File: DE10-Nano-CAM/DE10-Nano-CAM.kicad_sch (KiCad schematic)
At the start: 16 parts, among them J1 DF40C-100DS-0.4V_51_, J2 DF40C-100DS-0.4V_51_, J3 MEM2075-00-140-01-A, J4 Conn_02x20_Odd_Even, J5 52271-1579

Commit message: changed pcb
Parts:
- added R5, R6: 4.7k, Resistor_SMD:R_0603_1608Metric, symbol CAN-Adapter_3.2korr_0622-eagle-import:R-EU_R0603
- added R7, R8: DNP, Resistor_SMD:R_0603_1608Metric, symbol CAN-Adapter_3.2korr_0622-eagle-import:R-EU_R0603
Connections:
- net +3.3V: now also R5.2, R6.2, R7.2, R8.2
- net DATA_11: now also J4.21 (Pin_21); no longer J4.17 (Pin_17)
- net DDMI0_CLK_N: no longer J5.8
- net DDMI0_CLK_P: no longer J5.9
- net SCL0: now also R7.1
- net SDA0: now also R8.1
- net LVDS0_D0_P: now reaches J4.19 (Pin_19)
- net LVDS0_D0_P: now also J1.17
- net SCL_DE10: now reaches J4.31 (Pin_31)
- net SCL_DE10: now also R5.1
- net SDA_DE10: now reaches J4.32 (Pin_32)
- net SDA_DE10: now also R6.1
- net LVDS0_D1_N: now reaches J4.33 (Pin_33)
- net LVDS0_D1_N: now also J1.21
- net LVDS0_D2_N: now reaches J4.34 (Pin_34)
- net LVDS0_D2_N: now also J1.33
- net LVDS0_D1_P: now reaches J4.35 (Pin_35)
- net LVDS0_D1_P: now also J1.23
- net LVDS0_D2_P: now reaches J4.36 (Pin_36)
- net LVDS0_D2_P: now also J1.35
- net LVDS0_C_N: now reaches J4.37 (Pin_37)
- net LVDS0_C_N: now also J1.27
- net LVDS0_D3_N: now reaches J4.38 (Pin_38)
- net LVDS0_D3_N: now also J1.39
- net LVDS0_C_P: now reaches J4.39 (Pin_39)
- net LVDS0_C_P: now also J1.29
- net LVDS0_D3_P: now reaches J4.40 (Pin_40)
- net LVDS0_D3_P: now also J1.41
- net LVDS0_D0_N: now reaches J1.15
- net LVDS0_D0_N: now also J4.17 (Pin_17)
- new net LVDS1_C_N: J5.8
- new net LVDS1_C_P: J5.9
- no-connect marks 131 -> 108
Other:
- note added: "CONNECT TO WHERE?"
- note added: "Diff tuned to 14mm Diff Skew tuned"

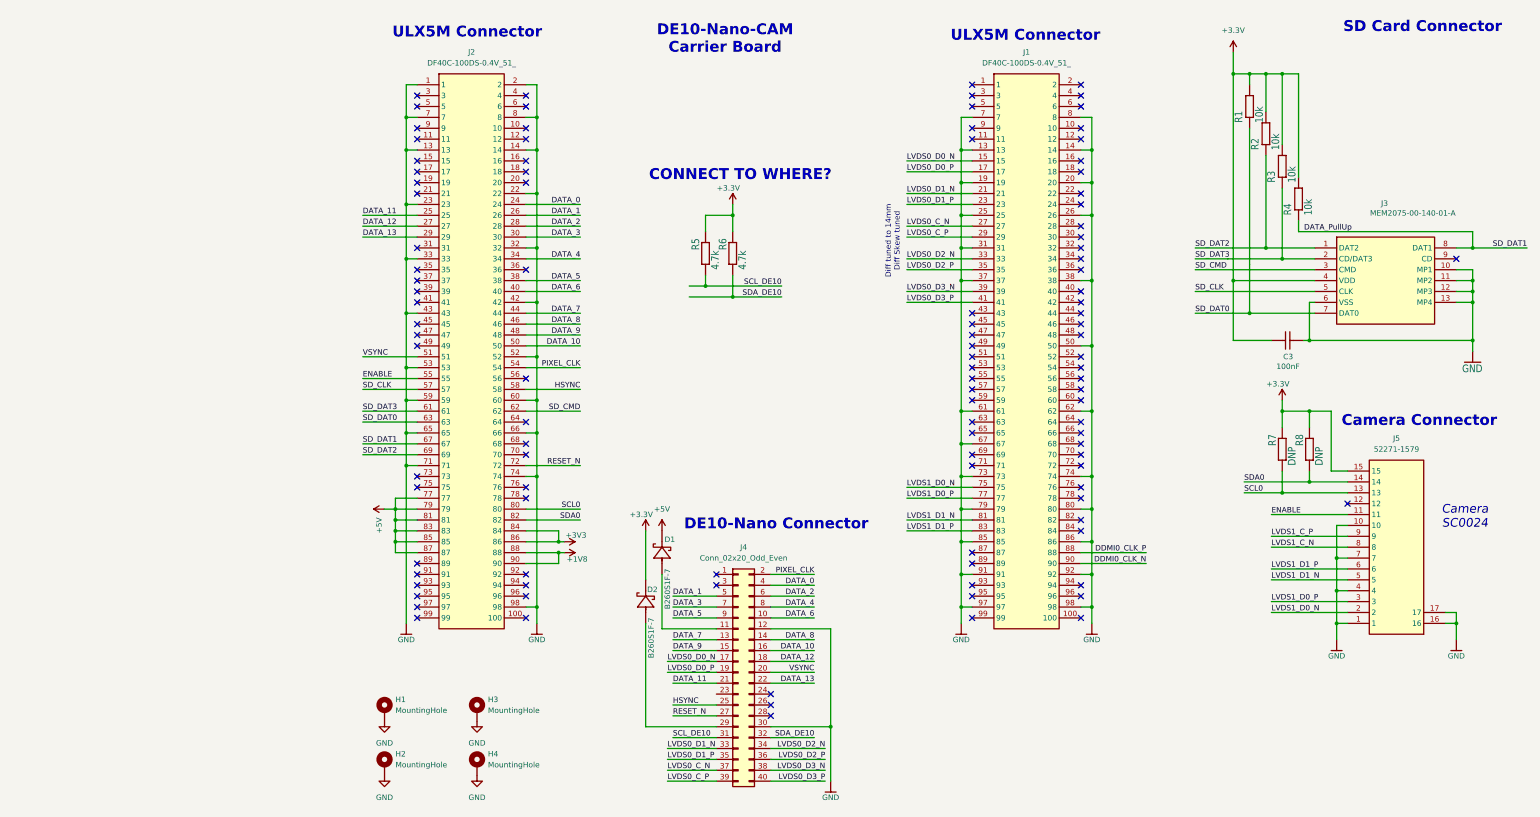
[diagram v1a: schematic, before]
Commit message: changes to DE10 schematic (GPIO)
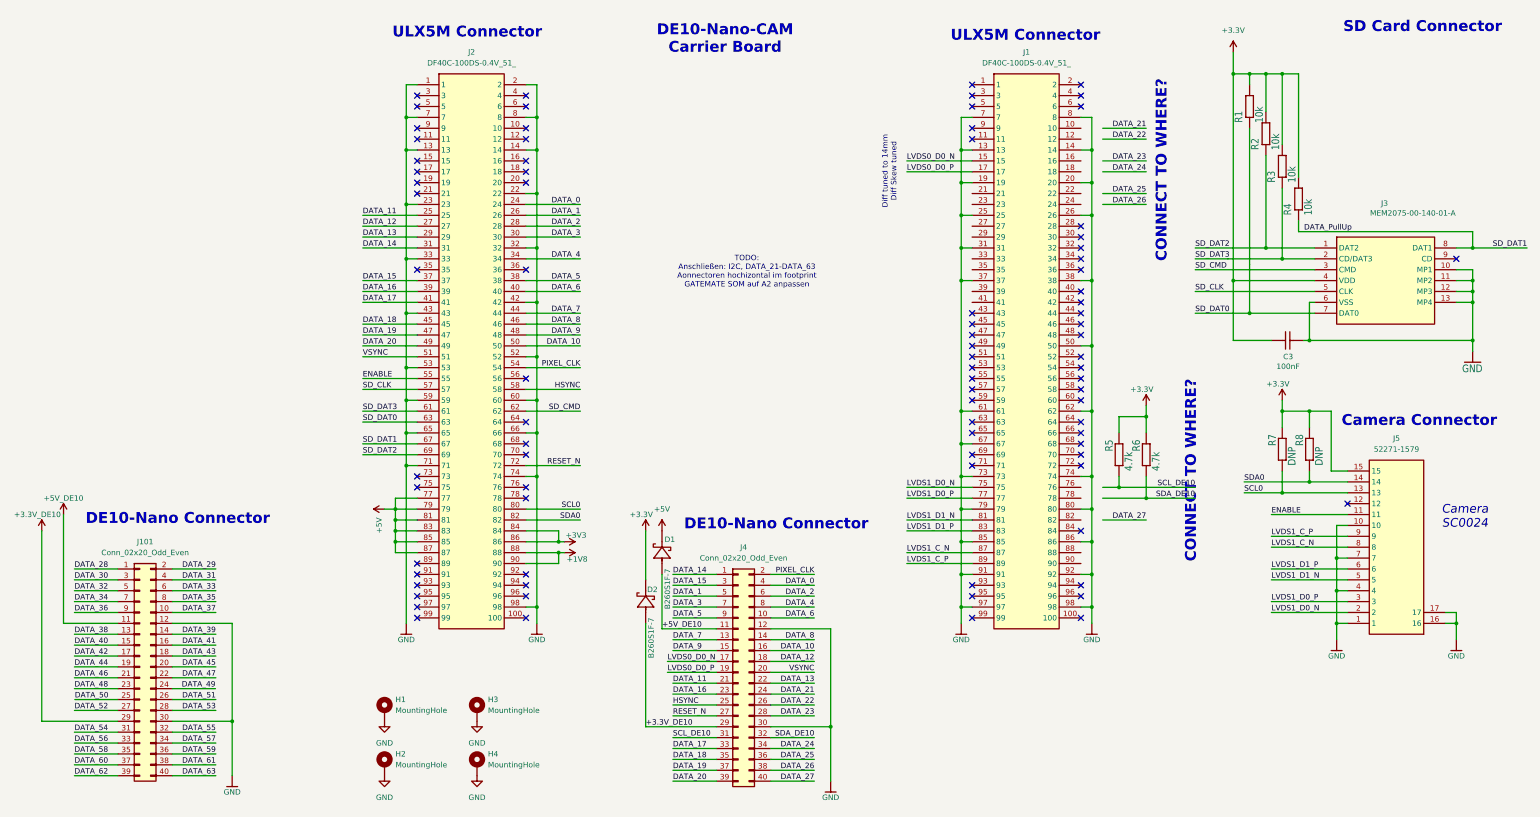
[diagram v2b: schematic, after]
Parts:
- added J101: Conn_02x20_Odd_Even, Connector_PinSocket_2.54mm:PinSocket_2x20_P2.54mm_Vertical, symbol Connector_Generic:Conn_02x20_Odd_Even
- J4: footprint Connector_PinSocket_2.54mm:PinSocket_2x20_P2.54mm_Horizontal -> Connector_PinSocket_2.54mm:PinSocket_2x20_P2.54mm_Vertical
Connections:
- net GND: now also J101.12 (Pin_12), J101.30 (Pin_30)
- net LVDS1_C_N: now also J1.87
- net LVDS1_C_P: now also J1.89
- net +3.3V_DE10: now reaches D2.2, J4.29 (Pin_29)
- net +3.3V_DE10: now also J101.29 (Pin_29)
- net DATA_14: now reaches J2.31
- net DATA_14: now also J4.1 (Pin_1)
- net DATA_15: now reaches J2.37
- net DATA_15: now also J4.3 (Pin_3)
- net DATA_16: now reaches J2.39
- net DATA_16: now also J4.23 (Pin_23)
- net DATA_17: now reaches J2.41
- net DATA_17: now also J4.33 (Pin_33)
- net DATA_18: now reaches J2.45
- net DATA_18: now also J4.35 (Pin_35)
- net DATA_19: now reaches J2.47
- net DATA_19: now also J4.37 (Pin_37)
- net DATA_20: now reaches J2.49
- net DATA_20: now also J4.39 (Pin_39)
- net +5V_DE10: now reaches D1.2, J4.11 (Pin_11)
- net +5V_DE10: now also J101.11 (Pin_11)
- net DATA_21: now reaches J4.24 (Pin_24)
- net DATA_22: now reaches J4.26 (Pin_26)
- net DATA_23: now reaches J4.28 (Pin_28)
- net DDMI0_CLK_N: no longer names the net of J1.90
- net DDMI0_CLK_P: no longer names the net of J1.88
- net LVDS0_C_N: no longer names the net of J1.27
- net LVDS0_C_N: no longer J4.37 (Pin_37)
- net LVDS0_C_P: no longer names the net of J1.29
- net LVDS0_C_P: no longer J4.39 (Pin_39)
- net LVDS0_D1_N: no longer names the net of J1.21
- net LVDS0_D1_N: no longer J4.33 (Pin_33)
- net LVDS0_D1_P: no longer names the net of J1.23
- net LVDS0_D1_P: no longer J4.35 (Pin_35)
- net LVDS0_D2_N: no longer names the net of J1.33
- net LVDS0_D2_N: no longer J4.34 (Pin_34)
- net LVDS0_D2_P: no longer names the net of J1.35
- net LVDS0_D2_P: no longer J4.36 (Pin_36)
- net LVDS0_D3_N: no longer names the net of J1.39
- net LVDS0_D3_N: no longer J4.38 (Pin_38)
- net LVDS0_D3_P: no longer names the net of J1.41
- net LVDS0_D3_P: no longer J4.40 (Pin_40)
- new net DATA_24: J4.34 (Pin_34)
- new net DATA_25: J4.36 (Pin_36)
- new net DATA_26: J4.38 (Pin_38)
- new net DATA_27: J4.40 (Pin_40)
- new net DATA_28: J101.1 (Pin_1)
- new net DATA_29: J101.2 (Pin_2)
- new net DATA_30: J101.3 (Pin_3)
- new net DATA_31: J101.4 (Pin_4)
- new net DATA_32: J101.5 (Pin_5)
- new net DATA_33: J101.6 (Pin_6)
- new net DATA_34: J101.7 (Pin_7)
- new net DATA_35: J101.8 (Pin_8)
- new net DATA_36: J101.9 (Pin_9)
- new net DATA_37: J101.10 (Pin_10)
- new net DATA_38: J101.13 (Pin_13)
- new net DATA_39: J101.14 (Pin_14)
- new net DATA_40: J101.15 (Pin_15)
- new net DATA_41: J101.16 (Pin_16)
- new net DATA_42: J101.17 (Pin_17)
- new net DATA_43: J101.18 (Pin_18)
- new net DATA_44: J101.19 (Pin_19)
- new net DATA_45: J101.20 (Pin_20)
- new net DATA_46: J101.21 (Pin_21)
- new net DATA_47: J101.22 (Pin_22)
- new net DATA_48: J101.23 (Pin_23)
- new net DATA_49: J101.24 (Pin_24)
- new net DATA_50: J101.25 (Pin_25)
- new net DATA_51: J101.26 (Pin_26)
- new net DATA_52: J101.27 (Pin_27)
- new net DATA_53: J101.28 (Pin_28)
- new net DATA_54: J101.31 (Pin_31)
- new net DATA_55: J101.32 (Pin_32)
- new net DATA_56: J101.33 (Pin_33)
- new net DATA_57: J101.34 (Pin_34)
- new net DATA_58: J101.35 (Pin_35)
- new net DATA_59: J101.36 (Pin_36)
- new net DATA_60: J101.37 (Pin_37)
- new net DATA_61: J101.38 (Pin_38)
- new net DATA_62: J101.39 (Pin_39)
- new net DATA_63: J101.40 (Pin_40)
- no-connect marks 108 -> 85
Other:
- note added: "TODO: Anschließen: I2C, DATA_21-DATA_63 Aonnectoren hochizontal im footprint GATEMATE SOM auf A2 anpassen"
- moved on the sheet: R5, R6

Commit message: changed PCB pinout
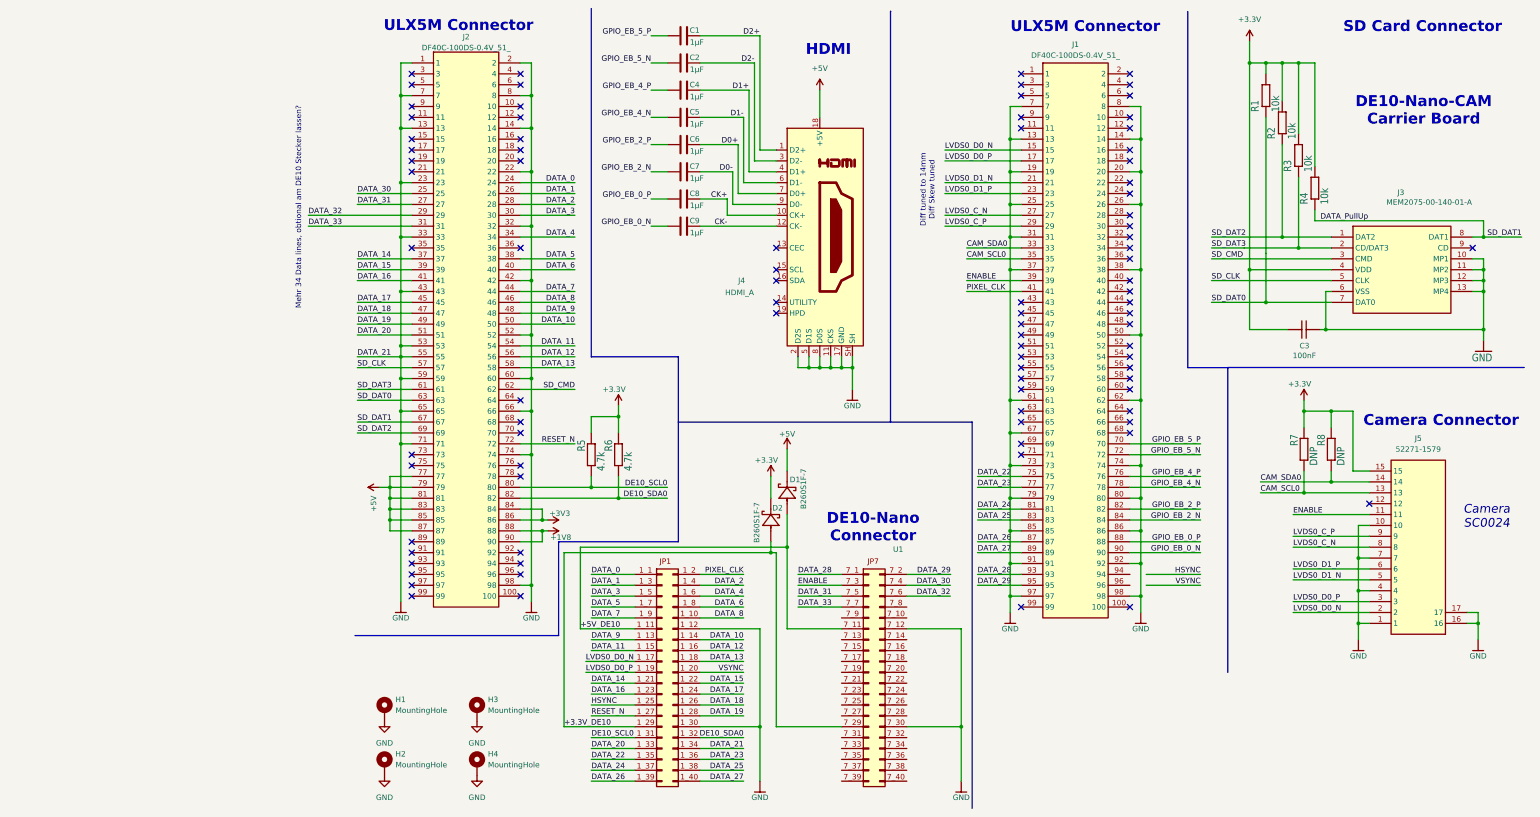
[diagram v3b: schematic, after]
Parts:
- removed J101, J4: Conn_02x20_Odd_Even, Connector_PinSocket_2.54mm:PinSocket_2x20_P2.54mm_Vertical, symbol Connector_Generic:Conn_02x20_Odd_Even
- added C1, C2, C4, C5, C6, C7, C8, C9: 1µF, Capacitor_SMD:C_0603_1608Metric_Pad1.08x0.95mm_HandSolder, symbol Device:C
- added J4: HDMI_A, Connector_Video:HDMI_A_Amphenol_10029449-x01xLF_Horizontal, symbol Connector:HDMI_A
- added U1: ~, Lib:DE10-Nano, symbol Lib:DE10_Nano
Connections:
- net +3.3V_DE10: now also U1.1_29, U1.7_29
- net +5V: now also J4.18 (+5V)
- net +5V_DE10: now also U1.1_11, U1.7_11
- net DATA_0: now also U1.1_1
- net DATA_1: now also U1.1_3
- net DATA_10: now also U1.1_14
- net DATA_11: now also J2.54, U1.1_15; no longer J2.25
- net DATA_12: now also J2.56, U1.1_16; no longer J2.27
- net DATA_13: now also J2.58, U1.1_18; no longer J2.29
- net DATA_14: now also J2.37, U1.1_21; no longer J2.31
- net DATA_15: now also J2.39, U1.1_22; no longer J2.37
- net DATA_16: now also J2.41, U1.1_23; no longer J2.39
- net DATA_17: now also J2.45, U1.1_24; no longer J2.41
- net DATA_18: now also J2.47, U1.1_26; no longer J2.45
- net DATA_19: now also J2.49, U1.1_28; no longer J2.47
- net DATA_2: now also U1.1_4
- net DATA_20: now also J2.51, U1.1_33; no longer J2.49
- net DATA_22: now also J1.75, U1.1_35
- net DATA_23: now also J1.77, U1.1_36
- net DATA_24: now also J1.81, U1.1_37
- net DATA_25: now also J1.83, U1.1_38
- net DATA_26: now also J1.87, U1.1_39
- net DATA_27: now also J1.89, U1.1_40
- net DATA_28: now also J1.93, U1.7_1
- net DATA_29: now also J1.95
- net DATA_3: now also U1.1_5
- net DATA_30: now also J2.25, U1.7_4
- net DATA_31: now also J2.27, U1.7_5
- net DATA_32: now also J2.29, U1.7_6
- net DATA_33: now also J2.31, U1.7_7
- net DATA_4: now also U1.1_6
- net DATA_5: now also U1.1_7
- net DATA_6: now also U1.1_8
- net DATA_7: now also U1.1_9
- net DATA_8: now also U1.1_10
- net DATA_9: now also U1.1_13
- net ENABLE: now also J1.39, U1.7_3; no longer J2.55
- net GND: now also J2.55, J4.11 (CKS), J4.17 (GND), J4.2 (D2S), J4.5 (D1S), J4.8 (D0S), J4.SH, U1.1_12, U1.1_30, U1.1_34
- net HSYNC: now also U1.1_25; no longer J2.58
- net LVDS0_D0_N: now also J5.2, U1.1_17
- net LVDS0_D0_P: now also J5.3, U1.1_19
- net PIXEL_CLK: now also J1.41, U1.1_2; no longer J2.54
- net RESET_N: now also U1.1_27
- net VSYNC: now also U1.1_20; no longer J2.51
- net LVDS0_D1_N: now reaches J1.21
- net LVDS0_D1_N: now also J5.5
- net LVDS0_D1_P: now reaches J1.23
- net LVDS0_D1_P: now also J5.6
- net LVDS0_C_N: now reaches J1.27
- net LVDS0_C_N: now also J5.8
- net LVDS0_C_P: now reaches J1.29
- net LVDS0_C_P: now also J5.9
- net CAM_SDA0: now reaches J1.33
- net CAM_SDA0: now also J5.14, R8.1
- net CAM_SCL0: now reaches J1.35
- net CAM_SCL0: now also J5.13, R7.1
- net GPIO_EB_5_P: now reaches J1.70
- net GPIO_EB_5_P: now also C1.1
- net GPIO_EB_5_N: now reaches J1.72
- net GPIO_EB_5_N: now also C2.1
- net GPIO_EB_4_P: now reaches J1.76
- net GPIO_EB_4_P: now also C4.1
- net GPIO_EB_4_N: now reaches J1.78
- net GPIO_EB_4_N: now also C5.1
- net GPIO_EB_2_P: now reaches J1.82
- net GPIO_EB_2_P: now also C6.1
- net GPIO_EB_2_N: now reaches J1.84
- net GPIO_EB_2_N: now also C7.1
- net GPIO_EB_0_P: now reaches J1.88
- net GPIO_EB_0_P: now also C8.1
- net GPIO_EB_0_N: now reaches J1.90
- net GPIO_EB_0_N: now also C9.1
- removed net LVDS1_C_N: J1.87, J5.8
- removed net LVDS1_C_P: J1.89, J5.9
- removed net LVDS1_D0_N: J1.75, J5.2
- removed net LVDS1_D0_P: J1.77, J5.3
- removed net LVDS1_D1_N: J1.81, J5.5
- removed net LVDS1_D1_P: J1.83, J5.6
- removed net SCL0: J2.80, J5.13, R7.1
- net SCL_DE10 renamed DE10_SCL0
- net DE10_SCL0: now also J2.80, U1.1_31
- removed net SDA0: J2.82, J5.14, R8.1
- net SDA_DE10 renamed DE10_SDA0
- net DE10_SDA0: now also J2.82, U1.1_32
- new net CK+: C8.2, J4.10 (CK+)
- new net CK-: C9.2, J4.12 (CK-)
- new net D0+: C6.2, J4.7 (D0+)
- new net D0-: C7.2, J4.9 (D0-)
- new net D1+: C4.2, J4.4 (D1+)
- new net D1-: C5.2, J4.6 (D1-)
- new net D2+: C1.2, J4.1 (D2+)
- new net D2-: C2.2, J4.3 (D2-)
- no-connect marks 85 -> 88
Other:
- note added: "HDMI"
- note added: "Mehr 34 Data lines, obtional am DE10 Stecker lassen?"
- note removed: "CONNECT TO WHERE?"
- note removed: "TODO: Anschließen: I2C, DATA_21-DATA_63 Aonnectoren hochizontal im footprint GATEMATE SOM auf A2 anpassen"
- moved on the sheet: C3, D1, D2, J1, J2, J3, J5, R1, R2, R3, R4, R5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

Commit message: changed minor pin fixes
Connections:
- net DATA_14: now also U1.1_17; no longer U1.1_21
- net DATA_15: now also U1.1_19; no longer U1.1_22
- net DATA_16: now also U1.1_21; no longer U1.1_23
- net DATA_17: now also U1.1_22; no longer U1.1_24
- net DATA_18: now also U1.1_23; no longer U1.1_26
- net DATA_19: now also U1.1_24; no longer U1.1_28
- net DATA_20: now also U1.1_26; no longer U1.1_33
- net DATA_22: now also U1.1_33; no longer U1.1_35
- net DATA_23: now also U1.1_34; no longer U1.1_36
- net DATA_24: now also U1.1_35; no longer U1.1_37
- net DATA_25: now also U1.1_36; no longer U1.1_38
- net DATA_26: now also U1.1_37; no longer U1.1_39
- net DATA_27: now also U1.1_38; no longer U1.1_40
- net DATA_28: now also U1.1_39; no longer U1.7_1
- net DATA_30: now also U1.7_2; no longer U1.7_4
- net DATA_31: now also U1.7_3; no longer U1.7_5
- net DATA_32: now also U1.7_4; no longer U1.7_6
- net DATA_33: now also U1.7_5; no longer U1.7_7
- net ENABLE: now also U1.7_1; no longer U1.7_3
- net GND: now also U1.1_28; no longer U1.1_34
- net HSYNC: now also J1.94
- net LVDS0_D0_N: no longer U1.1_17
- net LVDS0_D0_P: no longer U1.1_19
- net VSYNC: now also J1.96
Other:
- note removed: "Mehr 34 Data lines, obtional am DE10 Stecker lassen?"
